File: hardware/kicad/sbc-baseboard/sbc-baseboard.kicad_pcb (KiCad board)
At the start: 4 copper layers, 140 x 80 mm, 339 parts, among them J1 USB-C upstream, J10 RJ45 magjack 10/100, J11 COM/NO/NC, J12 COM/NO/NC, J13 Console, J14 +5V_TGT out, J15 GPIO + I2C, J16 SWD, J17 Qwiic PD, J18 PSU in (isolated), J19 PSU out (isolated), J2 USB-C PD in, J3 USB-C HID to target, J4 USB-A x2, J5 USB-A x2, J601 SWD (K20), J9 FTDI header, K801 G6K-2F-Y DC5, K802 G6K-2F-Y DC5, K803 JW1FSN-DC5V, Q101 2N7002, Q102 2N7002, Q801 2N7002, Q802 2N7002, Q803 AO3400A, SW201 RESET, SW601 DAP RESET, U101 STUSB4500QTR, U102 PCA9517A, U103 TPS54560BDDA, U104 TPS54560BDDA, U105 TPS62823DLC, U201 MK64FN1M0VLL12, U202 USBLC6-2SC6, U301 KSZ8081RNA, U401 USBLC6-2SC6, U402 USB2517, U403 TPS2553DBV, U404 TPS2553DBV, U405 TPS2553DBV, U406 TPS2553DBV, U407 TPS2553DBV, U408 USBLC6-2SC6, U409 USBLC6-2SC6, U410 USBLC6-2SC6, U411 USBLC6-2SC6, U501 FT231XS, U601 MK20DX128VFM5, U701 TXB0104PW, U702 TXB0108PW, U703 TXS0102DCU, U704 TPS26630RGE, U801 LTV-817, Y201 32.768kHz, Y301 25MHz, Y401 24MHz, Y601 8MHz

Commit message: Ground floods on both outer layers and 297 stitching vias over the routed board, from the standard's new copper pass
FLOODS and STITCH directives in gen/layout.py (GND on the plane's notched
outline top and bottom, PSU_GND inside the passthrough region, a 5 mm grid kept
out of the region by its creepage and stitched inside it inset by the same);
gen/pcb.py --copper runs the standard's tools/copper.py over the routed board
without regenerating placement. Floods cover 47 % of the top and 56 % of the
bottom; 2.7 ground vias per cm² outside the region; 142 connections left for
the hand pass; DRC at the 12 documented USB-C footprint errors, 35
starved-thermal warnings where the routing crowds a ground pad. Submodule to
the standards' step 11.

Co-Authored-By: Claude Fable 5.1 <noreply@anthropic.com>
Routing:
- net PSU_GND: vias 0 -> 30
- net GND: vias 6 -> 273
- added copper zone on B.Cu, net GND
- added copper zone on F.Cu, net GND
- added copper zone on B.Cu, net PSU_GND
- added copper zone on F.Cu, net PSU_GND

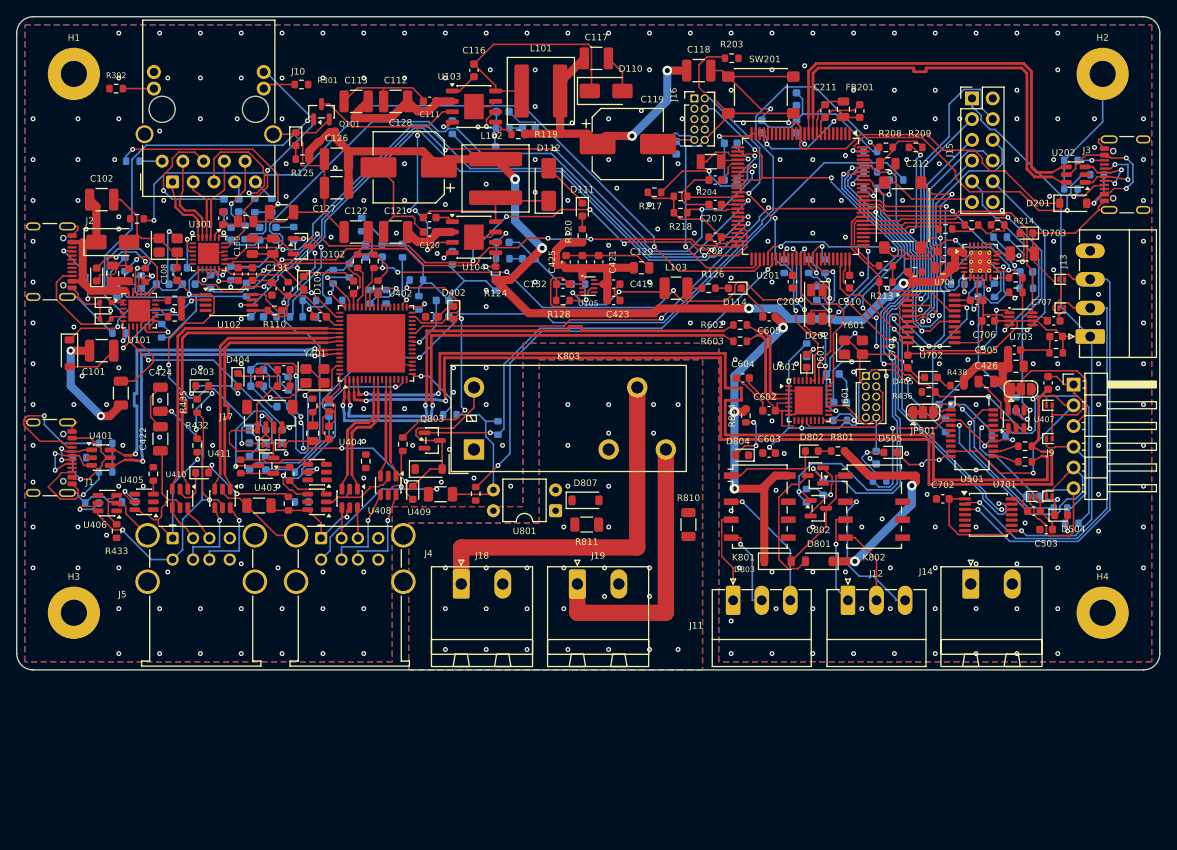
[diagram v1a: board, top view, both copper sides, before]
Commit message: The board grows to 140 x 100: routing discarded, 20 mm added below y 52, the front-edge blocks moved with the edge, placement recomputed
gen/layout.py: BOARD 140 x 100, H3/H4 at y 93, J1 at y 74, the USB-A stacks,
PSU terminals, relay terminals and J14 at the new front edge, the ESD arrays,
relays, eFuse, K803 and U801 20 mm down with them, the isolation region at
y 62-100 with its plane notch, rail rectangles, floods and stitching
rectangles, the PSU and port lanes' legs. Regenerated by the engine: 339
footprints, 0 parked, lanes matched to 0.00 mm, DRC at the 12 documented
footprint errors, 499 unrouted (no routing: the routed 140 x 80 board stays
at a94a986). Directives, spec, READMEs and the block diagram's mechanical
inset (now drawn from the edge table) follow; the standard's resize rule via
the submodule.

Co-Authored-By: Claude Fable 5.1 <noreply@anthropic.com>
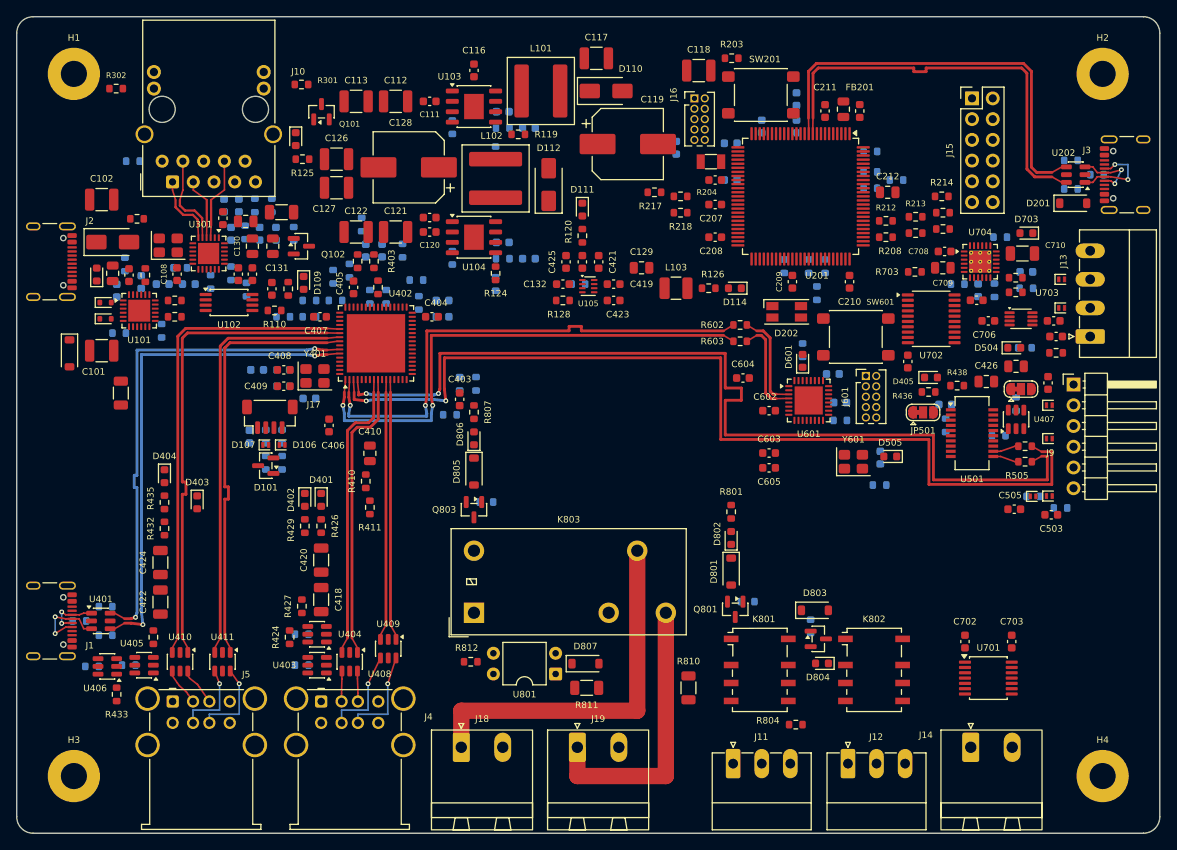
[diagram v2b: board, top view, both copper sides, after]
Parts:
- moved R804 38.3 mm to (95.4, 86.7), turned to 0 degrees
- moved D402 29.3 mm to (35.3, 59.2)
- moved D804 27.3 mm to (98.6, 79.2)
- moved R807 26.6 mm to (56.0, 48.4), turned to -90 degrees
- moved R502 22.3 mm to (123.5, 40.5)
- moved D504 21.3 mm to (122.2, 40.5)
- moved R405 21.0 mm to (54.2, 45.0)
- moved R812 20.6 mm to (55.6, 79.0), turned to 0 degrees
- moved R810 20.0 mm to (82.3, 82.2)
- moved R811 20.0 mm to (69.8, 82.2)
- moved R433 20.0 mm to (12.2, 83.0)
- moved R431 20.0 mm to (13.7, 79.4)
- moved U405 20.0 mm to (15.6, 79.4)
- moved R434 20.0 mm to (9.22, 79.6)
- moved U406 20.0 mm to (11.1, 79.6)
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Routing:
- net GND: track 702.0 -> 0.00 mm, vias 273 -> 0
- net +3V3: track 129.8 -> 0.00 mm
- net +5V_PORTS: track 126.8 -> 0.00 mm, vias 7 -> 0
- net +5V_TGT: track 122.0 -> 0.00 mm, vias 4 -> 0
- net VREF_TGT: track 120.7 -> 0.00 mm, vias 1 -> 0
- net PORT1_FAULT_N: track 118.1 -> 0.00 mm, vias 3 -> 0
- net FTDI_FAULT_N: track 110.7 -> 0.00 mm, vias 5 -> 0
- net MDIO: track 94.3 -> 0.00 mm, vias 2 -> 0
- net I2C0_SDA: track 91.2 -> 0.00 mm, vias 5 -> 0
- net RMII_RXER: track 88.8 -> 0.00 mm, vias 2 -> 0
- net +3V3_PD: track 87.9 -> 0.00 mm, vias 4 -> 0
- net RMII_TXEN: track 82.6 -> 0.00 mm, vias 2 -> 0
- net RMII_RXD0: track 82.5 -> 0.00 mm, vias 8 -> 0
- net RMII_TXD0: track 82.2 -> 0.00 mm, vias 2 -> 0
- net Net-(Q803-G): track 78.3 -> 0.00 mm, vias 1 -> 0
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- removed copper zone on B.Cu, net GND
- removed copper zone on F.Cu, net GND
- removed copper zone on B.Cu, net PSU_GND
- removed copper zone on F.Cu, net PSU_GND
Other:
- board size 140 x 80 mm -> 140 x 100 mm

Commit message: Placement follows the schematic's islands: 55 parts change host, the island spreads in the placement report
Regenerated with the standard's island rule (submodule bumped): port-switch
decoupling at the switches instead of the 3V3 buck, relay-driver resistors at
their transistors, crystal load capacitors at their crystals, the PD inlet
protection at J2, the 3V3 buck's output capacitors at the buck; ESD stays at
its connector. 55 islands of two or more parts, nine members more than 15 mm
from their island's centre (listed in placement.txt). DRC unchanged.

Co-Authored-By: Claude Fable 5.1 <noreply@anthropic.com>
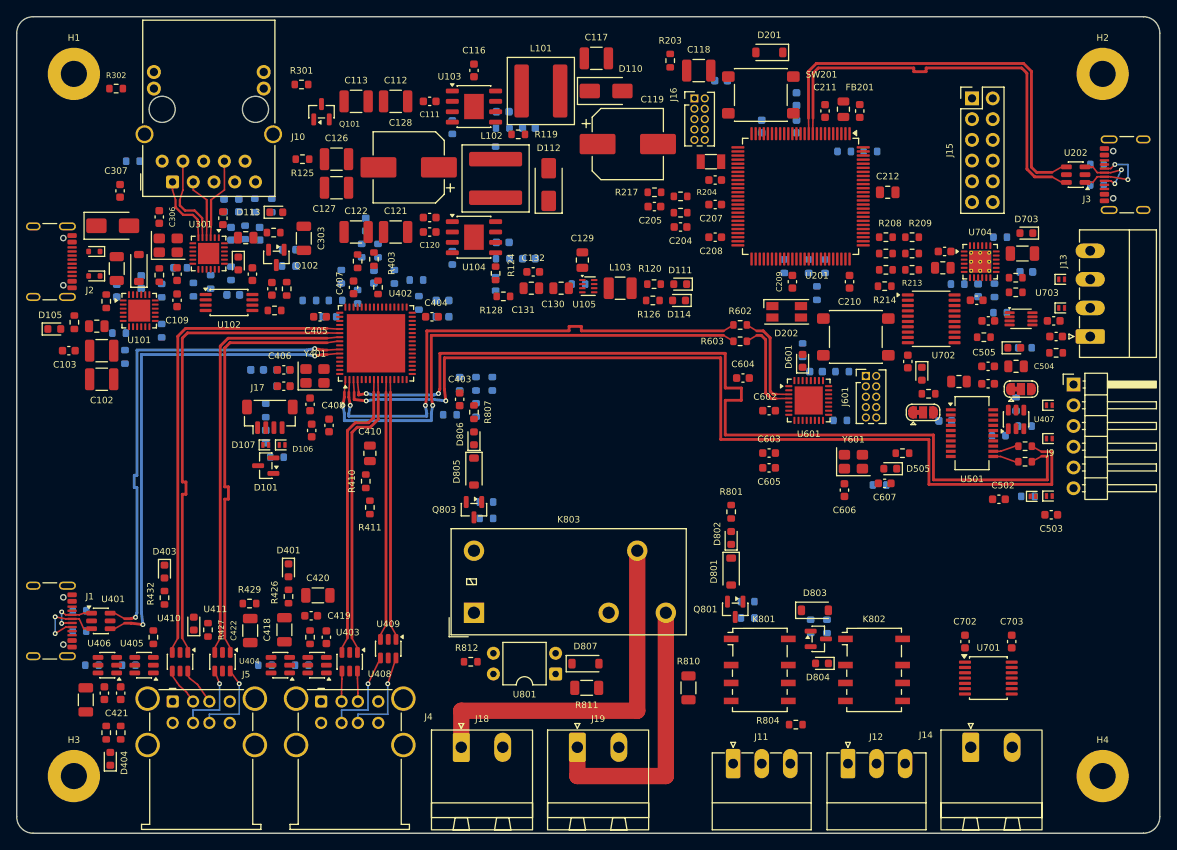
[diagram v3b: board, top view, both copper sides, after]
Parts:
- C204, C205, C306, C307, C415, C416, C606, C607: moved to F.Cu
- moved C421 78.8 mm to (12.7, 82.8), turned to -90 degrees
- moved C423 78.8 mm to (10.7, 82.8), turned to -90 degrees
- moved R809 65.1 mm to (57.5, 61.4), turned to 0 degrees
- moved R402 58.3 mm to (44.2, 28.6), turned to 90 degrees
- moved R806 55.9 mm to (99.2, 74.7), turned to 90 degrees
- moved C417 55.6 mm to (37.9, 76.0)
- moved C419 55.0 mm to (36.1, 73.4)
- moved R803 54.7 mm to (89.5, 73.6), turned to 0 degrees
- moved C425 53.8 mm to (119.0, 45.0), turned to 180 degrees
- moved D201 41.6 mm to (92.2, 4.37), turned to 180 degrees
- moved C130 38.2 mm to (66.7, 33.2), turned to 0 degrees
- moved D404 35.2 mm to (11.5, 90.9), turned to 90 degrees
- moved C131 32.1 mm to (63.0, 33.2), turned to 180 degrees
- moved R216 31.1 mm to (101.3, 16.5), turned to 180 degrees
- moved R435 29.1 mm to (11.0, 87.7), turned to -90 degrees
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
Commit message: The bucks as cities at the inlet: U103 and U104 stacked beside J2 with their circuits around them, 2 mm voids between every island
gen/layout.py: the RJ45 and PHY move right along the back edge (J10 at x 66,
U301 with it, J16 between the jack and the K64), the two 5 V bucks take the
inlet corner (U103 (24, 11), U104 (24, 27), loop flowing right), the 3V3 buck
sits at buck 1's output above the hub, the hub drops into the band the
taller board gained with its lanes' legs, the PD controller and buffer sit
below the bucks, the level shifters 2 mm apart; REGULATORS, CITY_GAP and a
plane void under the jack; the rails redrawn (5V_TGT across the band at
y 36-40 instead of the back edge). Regenerated: nothing parked, no gap
between cities narrower than 2 mm, two parts apart from their city, DRC at
the 12 documented footprint errors. Directives document, README and the
block diagram's inset follow; submodule to the standard's city rule.

Co-Authored-By: Claude Fable 5.1 <noreply@anthropic.com>
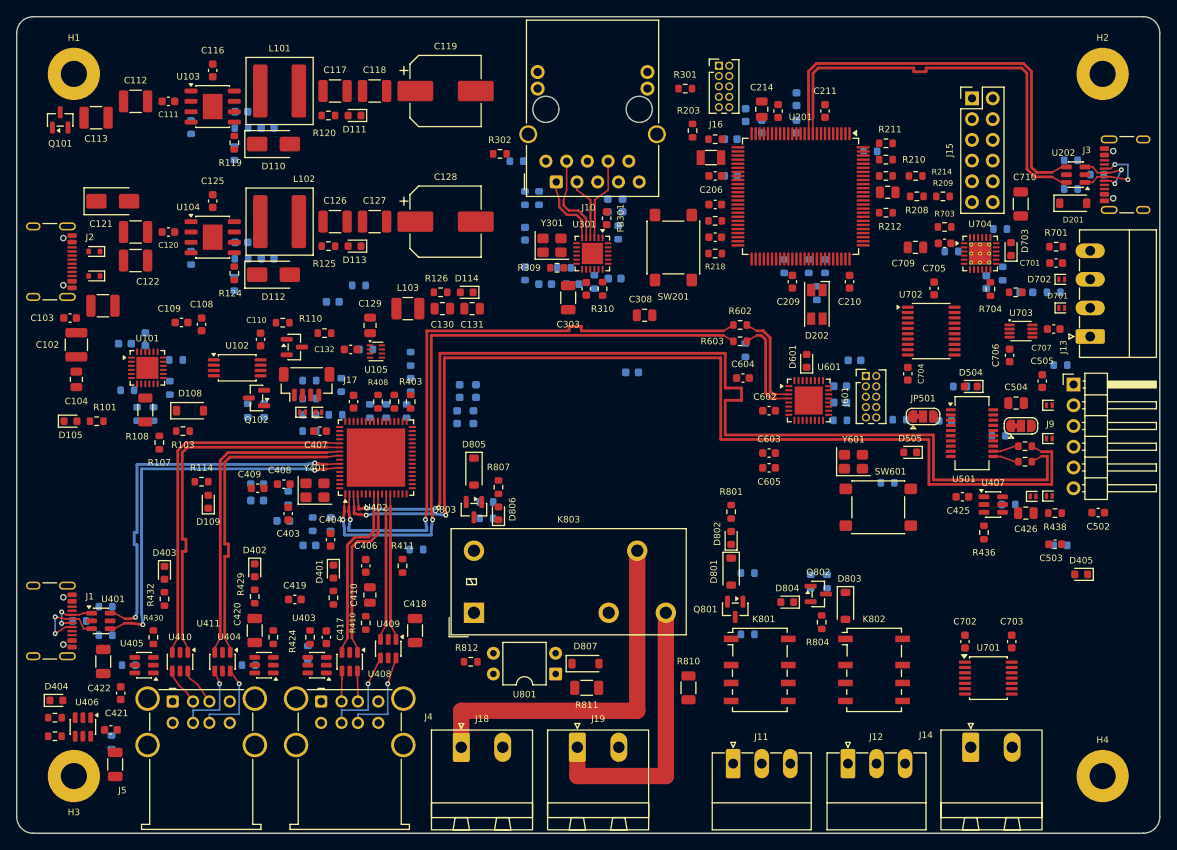
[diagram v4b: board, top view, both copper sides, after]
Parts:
- C204, C205, C306, C307, C415, C416, C606, C607: moved to B.Cu
- R114: moved to F.Cu
- moved R402 58.3 mm to (7.68, 74.0), turned to 180 degrees
- moved C307 53.3 mm to (64.7, 32.8), turned to 180 degrees
- moved C306 51.3 mm to (68.1, 32.8), turned to 180 degrees
- moved C309 49.8 mm to (75.4, 43.6)
- moved C308 49.8 mm to (76.9, 36.6)
- moved R302 47.7 mm to (59.2, 16.8)
- moved R301 47.0 mm to (81.9, 8.80)
- moved R311 47.0 mm to (67.0, 30.8)
- moved Y301 47.0 mm to (65.6, 28.0)
- moved C301 47.0 mm to (72.4, 23.1)
- moved C302 47.0 mm to (74.2, 23.1)
- moved FB301 47.0 mm to (72.2, 24.7)
- moved J10 47.0 mm to (66.1, 20.2)
- moved R306 47.0 mm to (61.2, 17.7)
- moved R307 47.0 mm to (70.8, 32.5)
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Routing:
- net /USB hub/HUB_UP_N: track 60.7 -> 46.7 mm
- net HUB_DN1_P: track 63.1 -> 77.1 mm
- net /USB hub/HUB_DN4_P: track 35.0 -> 21.0 mm
- net /USB hub/HUB_DN4_N: track 35.0 -> 21.0 mm
- net /USB hub/HUB_DN5_P: track 31.1 -> 17.1 mm
- net HUB_DN2_N: track 115.2 -> 129.2 mm
- net /USB hub/HUB_UP_P: track 60.7 -> 46.7 mm
- net /USB hub/HUB_DN7_P: track 51.9 -> 37.9 mm
- net /USB hub/HUB_DN7_N: track 51.8 -> 37.8 mm
- net /USB hub/HUB_DN6_P: track 58.2 -> 44.2 mm
- net /USB hub/HUB_DN6_N: track 58.2 -> 44.2 mm
- net /USB hub/HUB_DN5_N: track 31.1 -> 17.1 mm
- net HUB_DN1_N: track 63.1 -> 77.1 mm
- net HUB_DN2_P: track 115.2 -> 129.2 mm

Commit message: The three regulators placed from TI's layout examples: Figure 57 for the two bucks, Figure 52 for the 3V3 buck
gen/layout.py: LAYOUTS transcribe SLVSF00 Figure 57 (input column at VIN and
BOOT, catch diode along the side at SW, inductor beyond, output capacitors
above the inductor, RT below, compensation and divider right, all top side)
and SLVSDV6C Figure 52; the two bucks sit side by side along the back edge at
J2 (U103 (24, 24), U104 (52, 24)), the RJ45, PHY, SWD header and K64 move
right to make room, a plane void under the jack's courtyard, the rails
redrawn. Measured: diode 3.6 mm and inductor 6.9 mm from SW, bypass 2.1 mm
from VIN, RT 1.7 mm, nothing on the bottom, both bucks identical; voids
clean, nothing parked, DRC unchanged. Directives, guideline rows, README and
the block diagram follow; submodule to the standard's rule 3.2.

Co-Authored-By: Claude Fable 5.1 <noreply@anthropic.com>
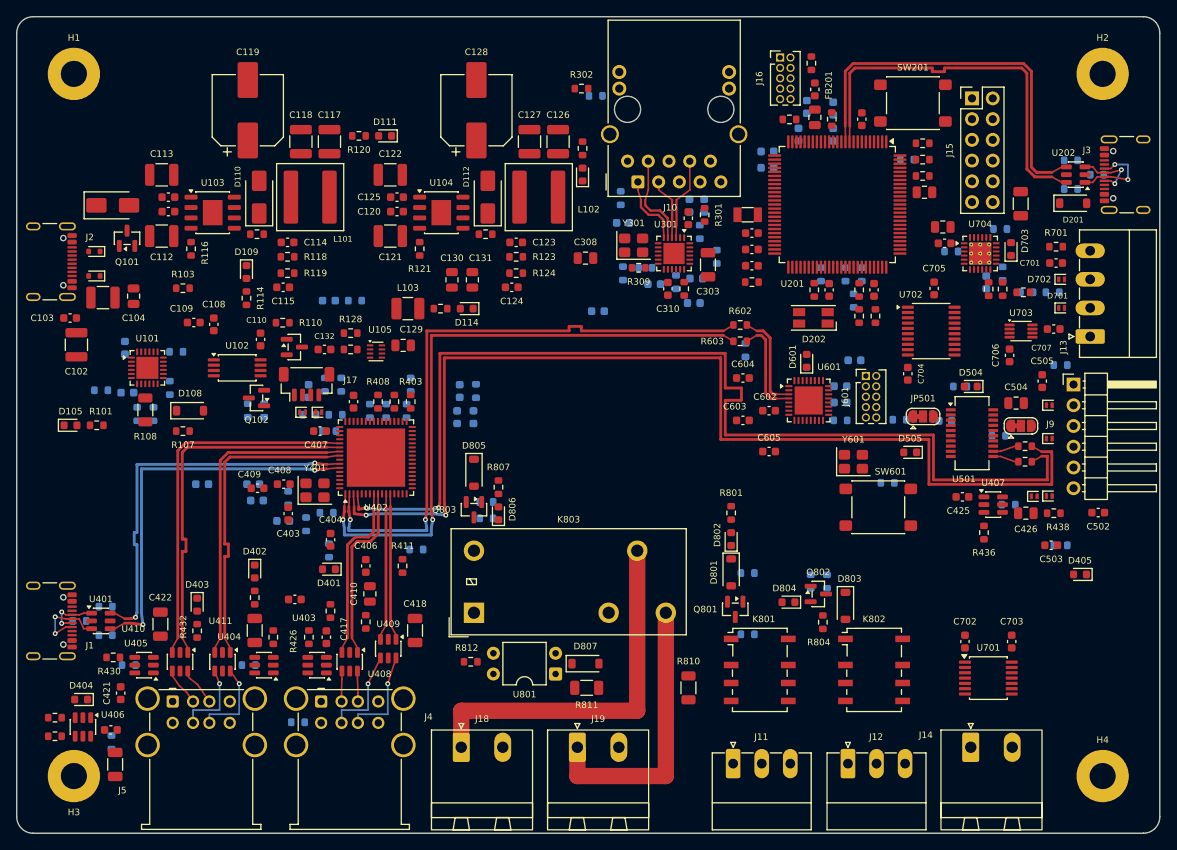
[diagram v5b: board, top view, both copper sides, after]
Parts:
- C114, C115, C123, C124, R116, R117, R118, R121, R122, R123, R127: moved to F.Cu
- moved R123 34.7 mm to (61.2, 29.4), turned to 0 degrees
- moved R124 34.5 mm to (61.2, 31.4), turned to 180 degrees
- moved SW201 34.3 mm to (109.8, 10.6), turned to 0 degrees
- moved C123 33.6 mm to (61.2, 27.6)
- moved R125 33.4 mm to (69.3, 16.1), turned to 90 degrees
- moved C122 32.9 mm to (45.8, 19.4)
- moved L102 31.9 mm to (63.9, 22.1)
- moved C121 31.2 mm to (45.8, 26.9)
- moved C124 30.1 mm to (60.6, 33.1)
- moved R122 30.1 mm to (57.4, 26.6)
- moved D113 29.3 mm to (69.3, 19.3), turned to 90 degrees
- moved C126 29.0 mm to (66.3, 15.3), turned to 90 degrees
- moved D109 28.5 mm to (28.1, 31.3), turned to -90 degrees
- moved U104 28.2 mm to (52.0, 24.0)
- moved C120 28.1 mm to (46.6, 23.9)
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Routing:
- net /MCU/K64_USB_P: track 50.9 -> 47.4 mm
- net /MCU/K64_USB_N: track 50.9 -> 47.4 mm
